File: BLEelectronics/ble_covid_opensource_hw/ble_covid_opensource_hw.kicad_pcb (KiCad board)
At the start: 2 copper layers, 40.7 x 31.3 mm, 72 parts, among them IC1 LTC4412xS6, IC2 LTC4054LES5-4.2#TRPBF, IC3 PCF8523T, IC4 MX25R6435FM2IL0, J1 USB_B_Micro, J2 Conn_01x01_Female, J3 Conn_02x05_Odd_Even, Q1 Si2307CDS, SW1 NO, SW2 SW_MEC_5G, U1 BAT-HLD-001, U2 ESD401, U3 ESD401, U4 LP5907MFX-3.3, U5 nRF52840, X1 32MHz, X2 32.768KHZ

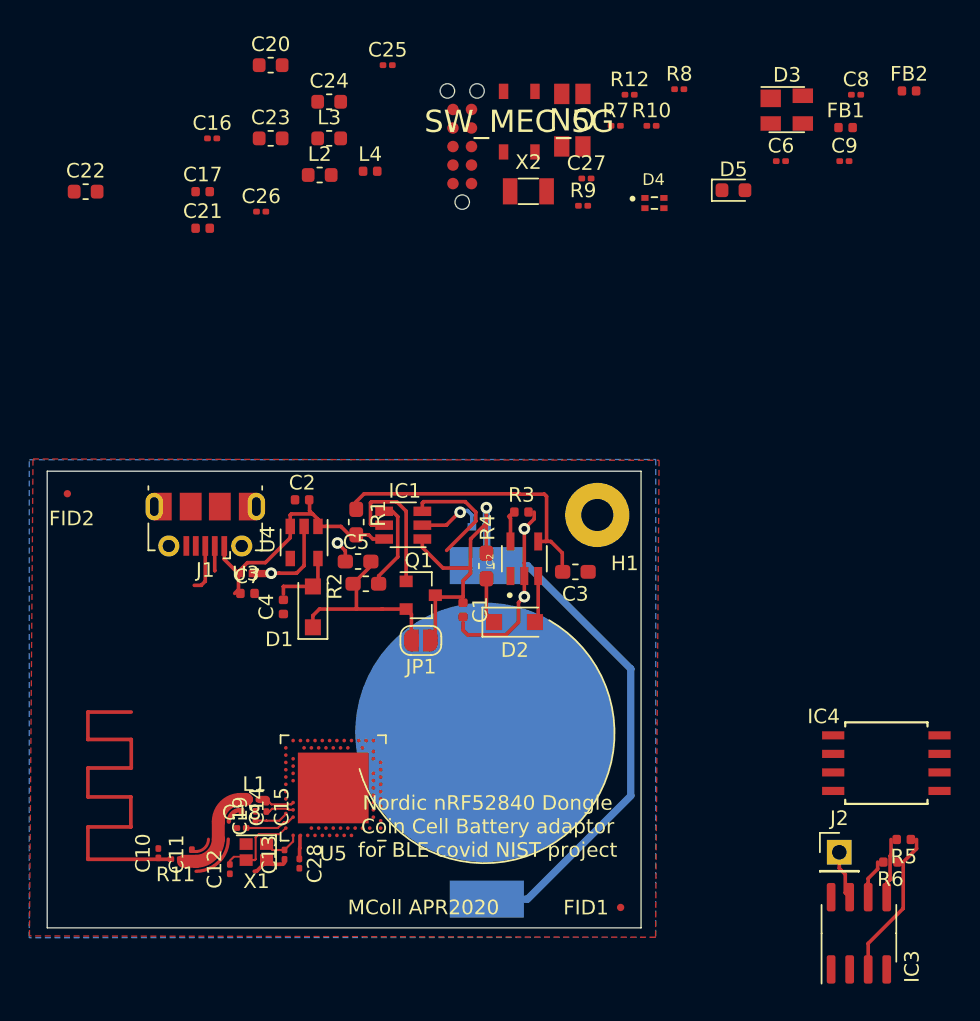
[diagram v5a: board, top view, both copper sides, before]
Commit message: hw mvp 1b all components on PCB, todo: traces.
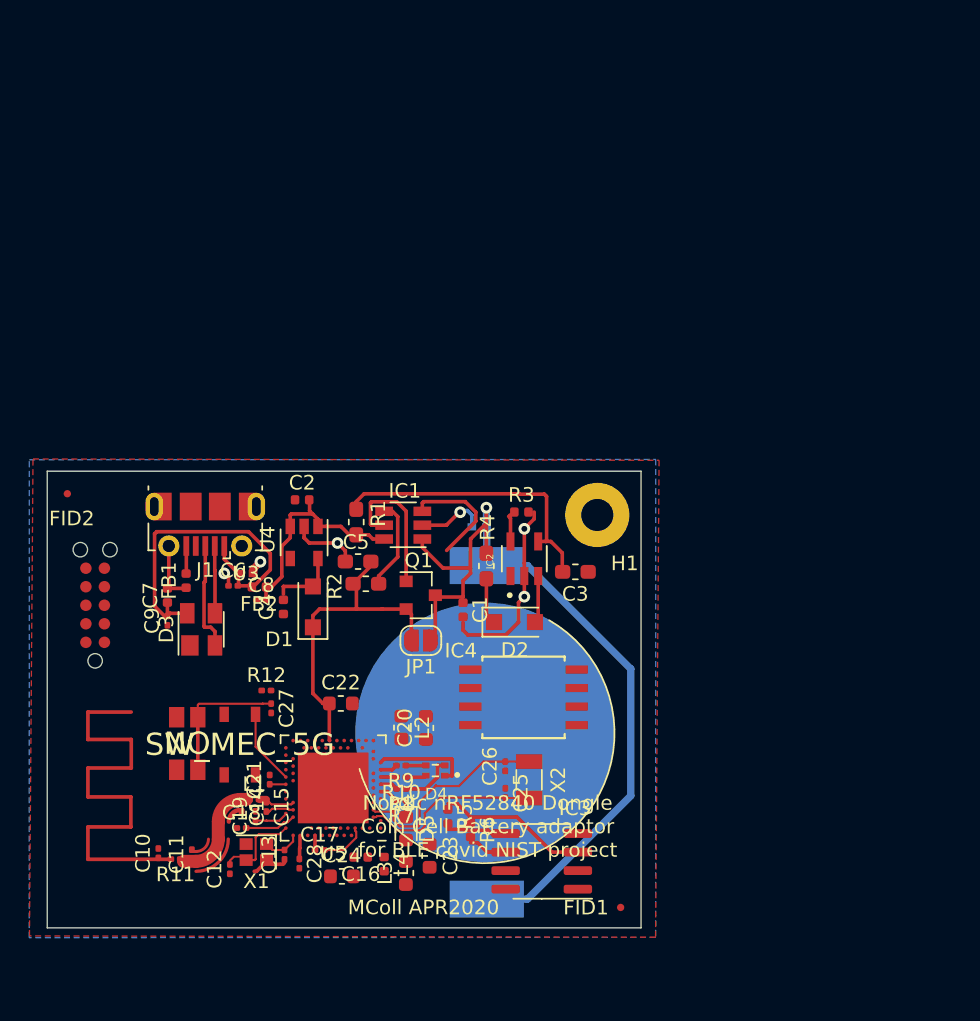
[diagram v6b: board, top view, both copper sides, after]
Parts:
- removed J2: Conn_01x01_Female, Connector_PinHeader_2.54mm:PinHeader_1x01_P2.54mm_Vertical
- C16: footprint Capacitor_SMD:C_0201_0603Metric -> Capacitor_SMD:C_0402_1005Metric
- C17, C21: footprint Capacitor_SMD:C_0402_1005Metric -> Capacitor_SMD:C_0201_0603Metric
- moved C9 56.1 mm to (132.5, 82.9), turned to 90 degrees
- moved FB2 56.0 mm to (138.8, 80.6), turned to 180 degrees
- moved FB1 54.8 mm to (133.8, 80.2), turned to 90 degrees
- moved D3 53.7 mm to (134.8, 83.5), turned to 90 degrees
- moved C8 53.5 mm to (139.0, 81.6)
- moved C24 53.1 mm to (144.5, 100.5)
- moved R8 51.6 mm to (148.6, 94.5), turned to 180 degrees
- moved L3 50.6 mm to (148.9, 100.2), turned to 90 degrees
- moved C25 50.5 mm to (155.7, 94.8), turned to 270 degrees
- moved C23 50.4 mm to (150.5, 99.1), turned to 270 degrees
- moved C16 50.3 mm to (145.8, 99.1), turned to 180 degrees
- moved SW1 50.2 mm to (133.9, 91.4)
- moved D5 49.2 mm to (148.9, 97.2), turned to 270 degrees
- moved R7 48.5 mm to (148.6, 95.3), turned to 180 degrees
- moved R10 47.8 mm to (148.6, 93.7), turned to 180 degrees
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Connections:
- L3 pad 1: Net-(C19-Pad1) -> Net-(L3-Pad1)
- L3 pad 2: Net-(L3-Pad2) -> Net-(C24-Pad1)
- L4 pad 1: Net-(L3-Pad2) -> Net-(C19-Pad1)
- L4 pad 2: Net-(C24-Pad1) -> Net-(L3-Pad1)
- U3 pad 1: /5Vusb -> Net-(C6-Pad2)
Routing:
- net Net-(C6-Pad2): track 0.00 -> 24.2 mm
- net /VDD_3V: track 23.8 -> 39.0 mm
- net Net-(C26-Pad2): track 0.00 -> 14.4 mm
- net Net-(C25-Pad2): track 0.00 -> 12.6 mm
- net /nRF52840_QIAA_R/RESET: track 0.00 -> 9.51 mm
- net GND: track 38.2 -> 44.4 mm, vias 5 -> 6
- net /nRF52840_QIAA_R/SW1: track 0.00 -> 5.16 mm
- net /D+: track 3.29 -> 7.40 mm
- net Net-(D4-Pad2): track 0.00 -> 3.80 mm
- net Net-(IC3-Pad7): track 3.37 -> 0.00 mm
- net /5Vusb: track 18.5 -> 15.3 mm
- net /D-: track 1.70 -> 4.63 mm
- net Net-(FB1-Pad2): track 0.00 -> 1.90 mm
- net Net-(D4-Pad4): track 0.00 -> 1.41 mm
- net Net-(D4-Pad3): track 0.00 -> 1.38 mm
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
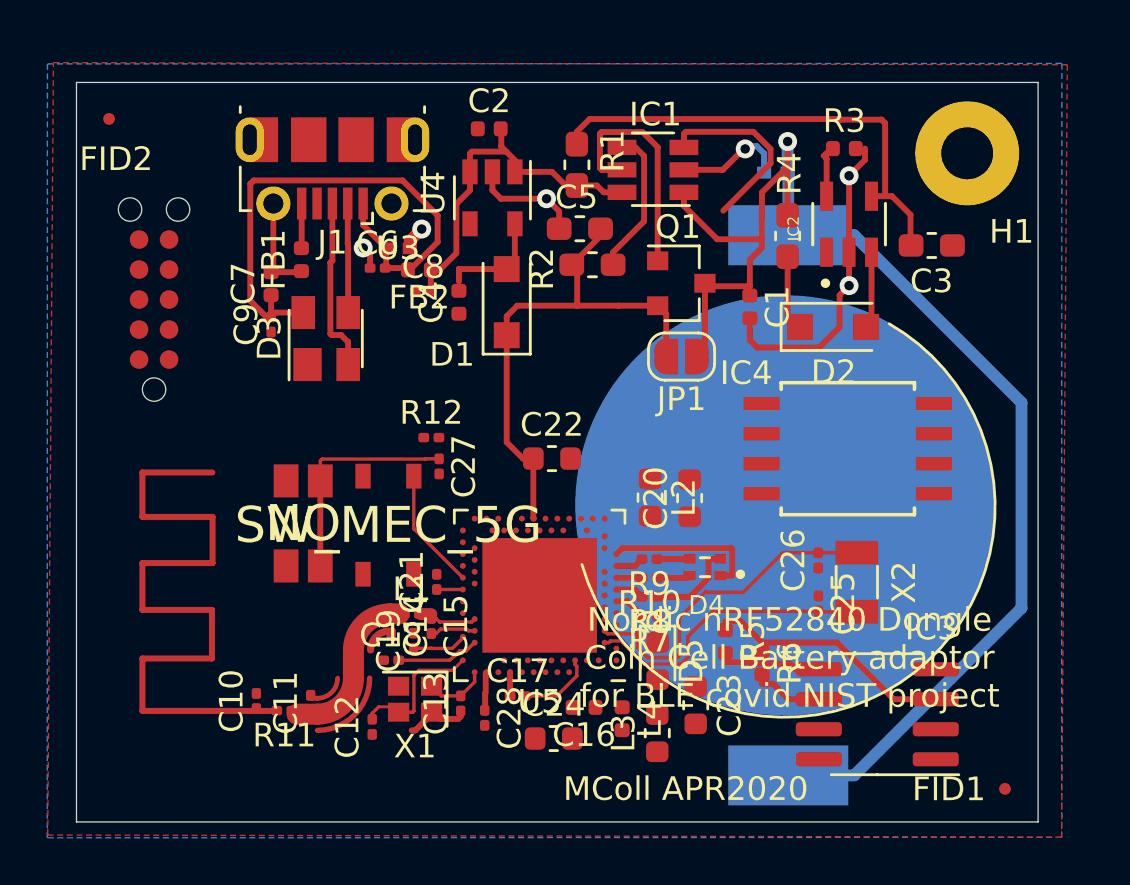
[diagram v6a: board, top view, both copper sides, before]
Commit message: schematic updated to be close to the Dongle. Layout update to closer to final footprint. Some traces todo.
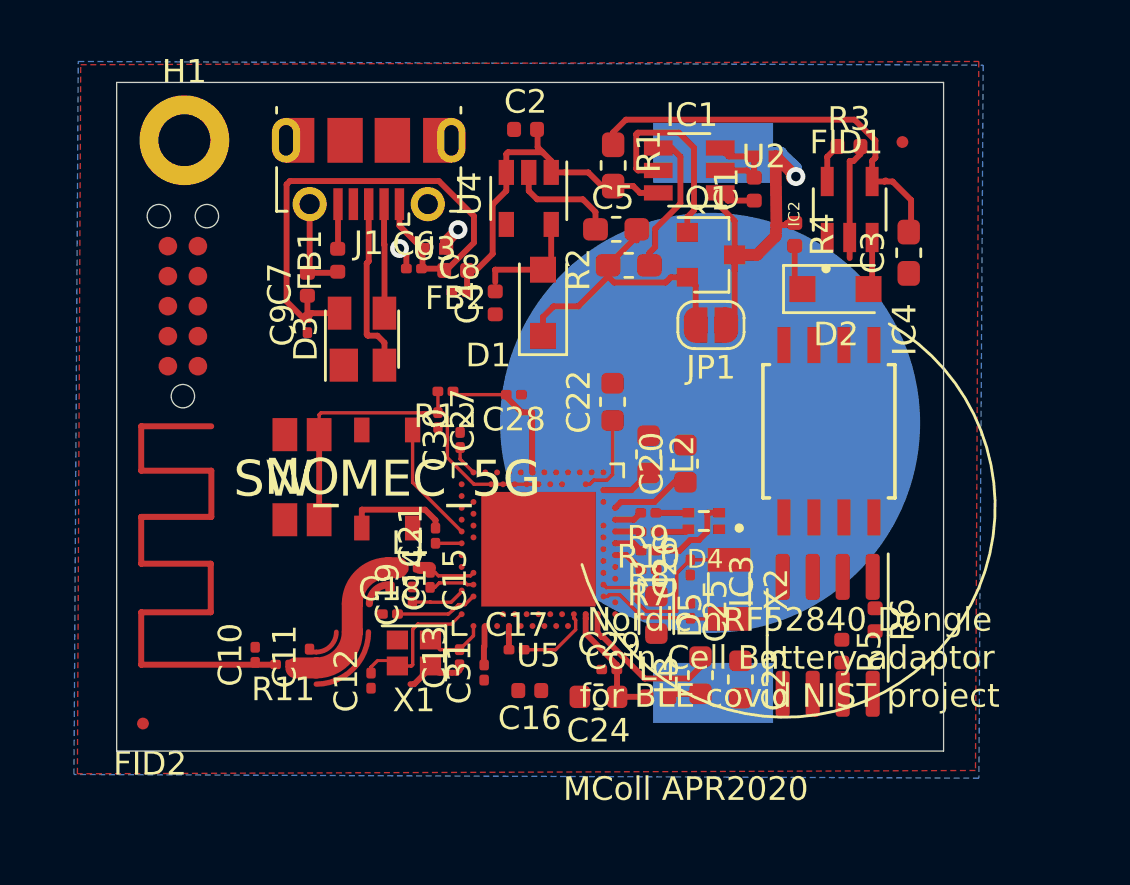
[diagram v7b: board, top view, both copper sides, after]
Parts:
- added C29: 47nF, Capacitor_SMD:C_0201_0603Metric, F.Cu at (146.9, 97.5)
- added C30: 100nF, Capacitor_SMD:C_0201_0603Metric, F.Cu at (140.5, 87.8)
- added C31: 100nF, Capacitor_SMD:C_0201_0603Metric, F.Cu at (141.6, 97.7)
- H1: footprint MountingHole:MountingHole_2.2mm_M2_Pad -> MountingHole:MountingHole_2.2mm_M2_DIN965_Pad
- R4: footprint Resistor_SMD:R_0603_1608Metric_Pad1.05x0.95mm_HandSolder -> Resistor_SMD:R_0402_1005Metric
- U2: moved to F.Cu
- moved H1 33.1 mm to (128.9, 75.1)
- moved FID1 27.7 mm to (159.3, 75.2)
- moved FID2 25.6 mm to (127.1, 99.8)
- moved C28 13.7 mm to (142.8, 85.9), turned to 180 degrees
- moved C25 5.42 mm to (150.3, 95.1)
- moved C26 5.42 mm to (150.3, 93.2)
- moved X2 5.42 mm to (151.9, 94.2)
- moved R6 5.13 mm to (158.1, 95.4)
- moved C1 4.99 mm to (153.0, 77.2), turned to 90 degrees
- moved R5 4.94 mm to (156.7, 96.8)
- moved U1 4.72 mm to (151.1, 87.1)
- moved IC3 3.95 mm to (156.1, 96.1), turned to 270 degrees
- moved C22 3.51 mm to (147.0, 86.2), turned to 90 degrees
- moved L3 3.06 mm to (150.7, 97.8)
- moved C24 2.59 mm to (146.4, 98.7), turned to 180 degrees
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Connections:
- C20 pad 1: Net-(C20-Pad1) -> /VDD_3V
- C22 pad 1: /VDD_3V -> Net-(C22-Pad1)
- C23 pad 1: /VDD_3V -> GND
- C23 pad 2: GND -> /VDD_3V
- C24 pad 1: Net-(C24-Pad1) -> Net-(C19-Pad1)
- C28 pad 1: Net-(C28-Pad1) -> GND
- C28 pad 2: GND -> /VDD_3V
- L3 pad 2: Net-(C24-Pad1) -> Net-(L3-Pad2)
- U1 pad 1: Net-(U1-Pad1) -> /3V
- U1 pad 3: Net-(U1-Pad1) -> /3V
- U2 pad 2: Net-(U1-Pad1) -> /3V
- U5 pad A14: Net-(U5-PadA14) -> /RESET
- U5 pad A22: Net-(C28-Pad1) -> /VDD_3V
- U5 pad AC15: /SCLK -> /nRF52840_QIAA_R/RESET
- U5 pad AC17: /SO -> /nRF52840_QIAA_R/RESET
- U5 pad AC19: /RESET -> /nRF52840_QIAA_R/RESET
- U5 pad AC21: Net-(U5-PadAC21) -> /nRF52840_QIAA_R/RESET
- U5 pad AC5: Net-(C20-Pad1) -> Net-(C22-Pad1)
- U5 pad AD10: /SCL -> /SO
- U5 pad AD12: /CS -> /SCLK
- U5 pad AD16: /SI -> /WP
- U5 pad AD18: /WP -> /SI
- U5 pad AD22: Net-(U5-PadAD22) -> /SCL
- U5 pad AD23: /VDD_3V -> Net-(C30-Pad1)
- U5 pad AD8: Net-(U5-PadAD8) -> /CS
- U5 pad B3: Net-(C24-Pad1) -> Net-(L3-Pad2)
- U5 pad EP: GND -> Net-(U5-PadEP)
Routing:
- net /3V: track 57.1 -> 20.2 mm
- net /VDD_3V: track 39.0 -> 24.7 mm
- net GND: track 44.4 -> 32.3 mm, vias 6 -> 2
- net /nRF52840_QIAA_R/RESET: track 9.51 -> 16.9 mm
- net Net-(C25-Pad2): track 12.6 -> 5.73 mm
- net Net-(L3-Pad2): track 0.00 -> 6.59 mm
- net Net-(C26-Pad2): track 14.4 -> 8.04 mm
- net Net-(C19-Pad1): track 2.23 -> 7.99 mm
- net /SDA: track 4.08 -> 0.00 mm
- net Net-(C22-Pad1): track 0.00 -> 3.60 mm
- net Net-(C3-Pad1): track 20.2 -> 17.3 mm
- net /SCL: track 2.67 -> 0.00 mm
- net Net-(L2-Pad2): track 0.00 -> 2.21 mm
- net Net-(C28-Pad1): track 1.71 -> 0.00 mm
- net Net-(L3-Pad1): track 0.00 -> 1.37 mm
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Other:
- board size 40.7 x 31.3 mm -> 35 x 28.3 mm

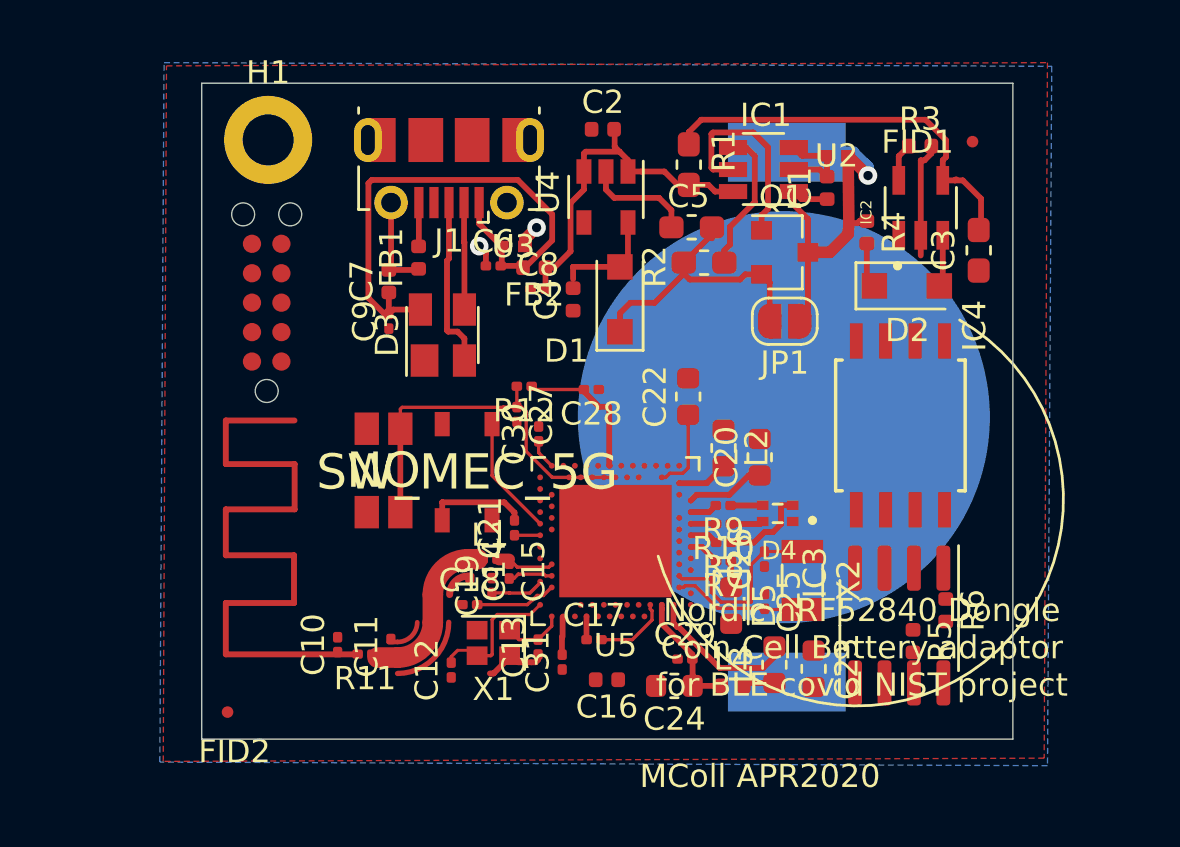
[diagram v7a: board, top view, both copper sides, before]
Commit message: hw mvp 1b layout full draft. Antenna still throwing DRC errors to be checked.
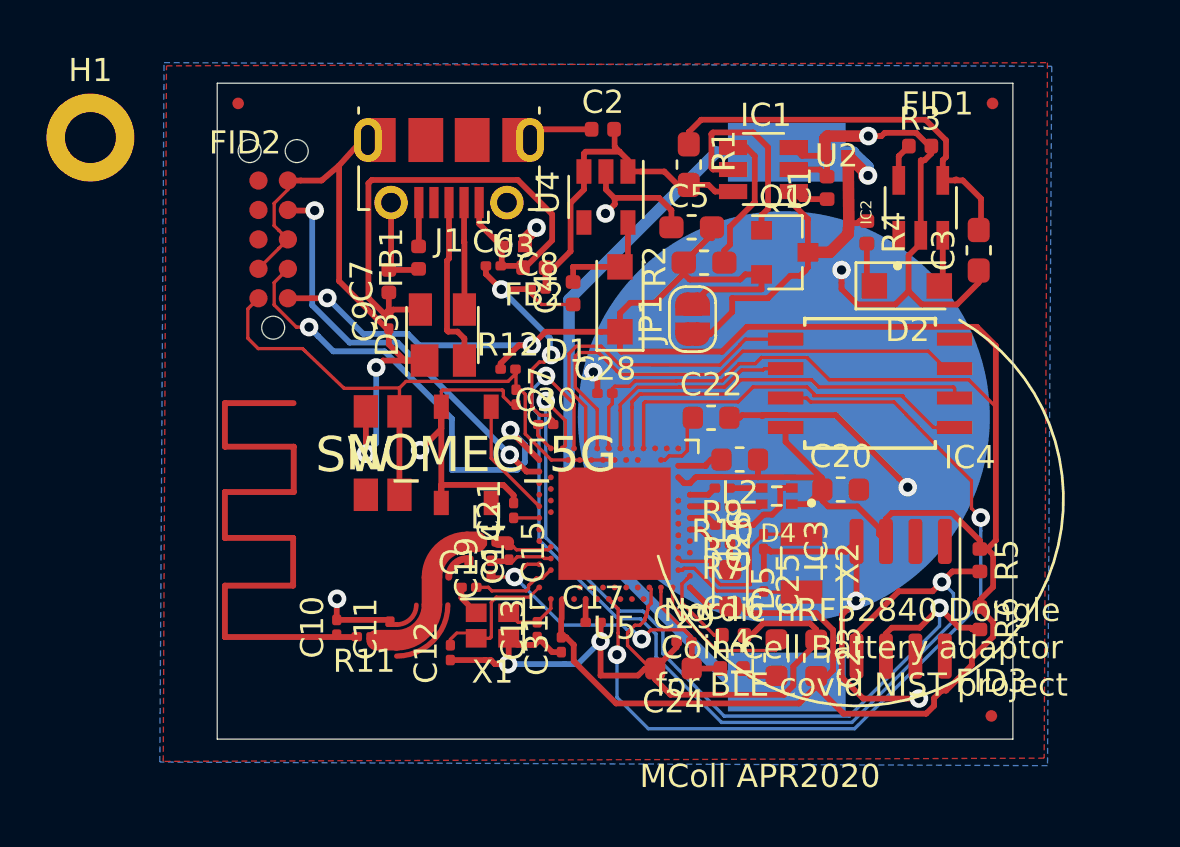
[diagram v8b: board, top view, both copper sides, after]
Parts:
- added FID3: Fiducial, Fiducial:Fiducial_0.5mm_Mask1mm, F.Cu at (160.1, 100.0)
- moved FID2 26.3 mm to (127.6, 73.6)
- moved H1 7.67 mm to (121.2, 75.0)
- moved C16 5.78 mm to (148.9, 96.5), turned to 0 degrees
- moved R5 4.53 mm to (159.6, 93.3)
- moved JP1 3.98 mm to (147.2, 82.9), turned to 90 degrees
- moved C20 3.76 mm to (153.6, 90.2), turned to 0 degrees
- moved J3 2.74 mm to (129.1, 79.4)
- moved IC4 2.24 mm to (154.8, 85.6), turned to 180 degrees
- moved FID1 1.86 mm to (160.1, 73.6)
- moved R6 1.51 mm to (159.6, 95.8)
- moved C22 1.35 mm to (148.0, 87.1), turned to 0 degrees
- moved IC3 1.16 mm to (156.2, 94.9)
- moved R12 1.02 mm to (139.2, 85.0), turned to 0 degrees
- moved L2 0.86 mm to (149.2, 88.9), turned to 180 degrees
- moved C15 0.81 mm to (139.3, 92.9)
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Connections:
- net /RESET renamed /SIO3
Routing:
- net GND: track 32.3 -> 163.1 mm, vias 2 -> 16
- net /VDD_3V: track 24.7 -> 148.3 mm, vias 0 -> 2
- net /SDA: track 0.00 -> 43.9 mm, vias 0 -> 2
- net /SIO3: track 0.00 -> 37.9 mm, vias 0 -> 2
- net /SCL: track 0.00 -> 37.4 mm, vias 0 -> 2
- net /3V: track 20.2 -> 57.4 mm
- net /WP: track 0.00 -> 21.8 mm
- net /nRF52840_QIAA_R/SWDIO: track 0.00 -> 20.5 mm, vias 0 -> 2
- net /nRF52840_QIAA_R/SWDCLK: track 0.00 -> 18.1 mm, vias 0 -> 2
- net /SO: track 0.00 -> 17.1 mm
- net /CS: track 0.00 -> 16.5 mm
- net /SI: track 0.00 -> 14.7 mm
- net /nRF52840_QIAA_R/RESET: track 16.9 -> 26.8 mm
- net /SCLK: track 0.00 -> 9.71 mm
- net Net-(C19-Pad1): track 7.99 -> 17.1 mm, vias 0 -> 2
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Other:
- board size 35 x 28.3 mm -> 34.3 x 28.3 mm
